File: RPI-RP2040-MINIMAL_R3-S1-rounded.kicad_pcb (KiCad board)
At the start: 2 copper layers, 65 x 46.7 mm, 34 parts, among them J1 Conn_01x03_Socket, J3 Conn_01x04_Pin, J4 Conn_01x04_Socket, P1 USB_C_Plug_USB2.0, U1 NCP1117ST33T3G, U2 W25Q128JVSIQ, U3 RP2040, X1 12MHz

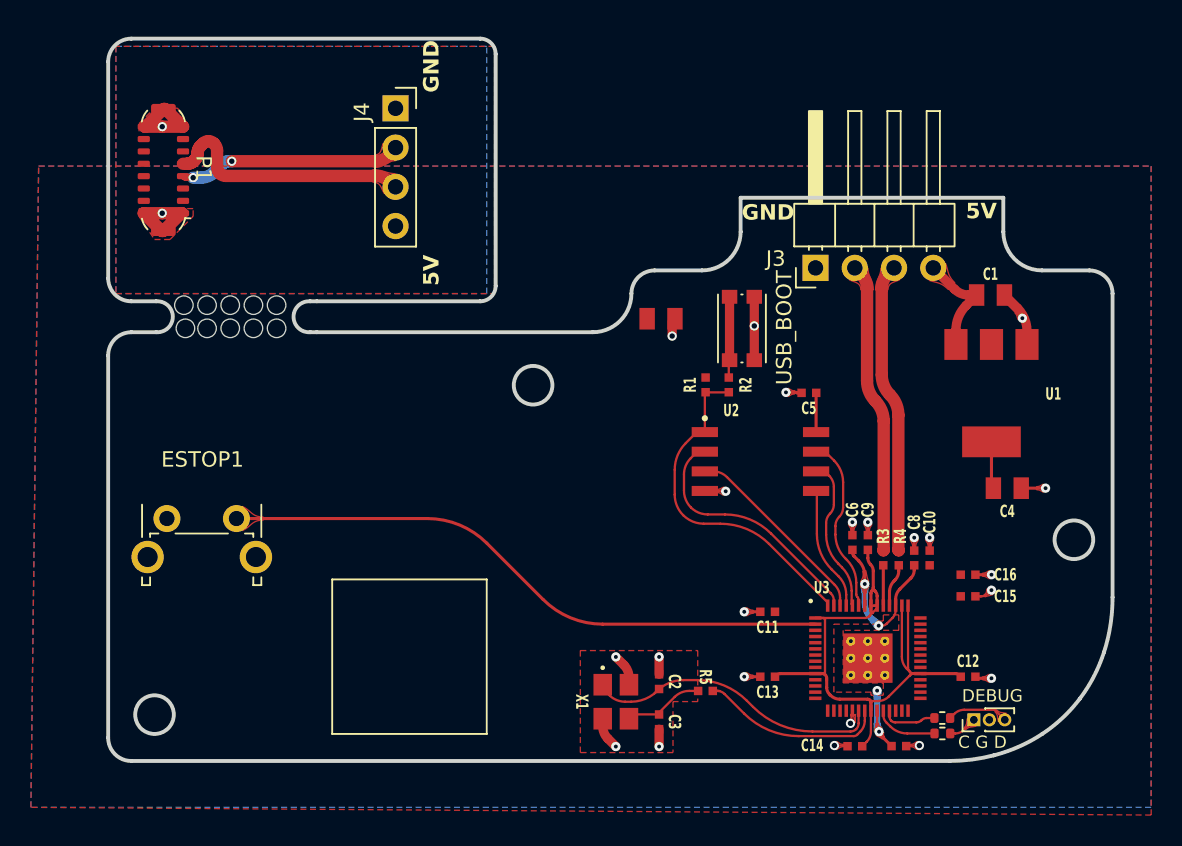
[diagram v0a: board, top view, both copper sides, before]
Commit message: attach both sides of port
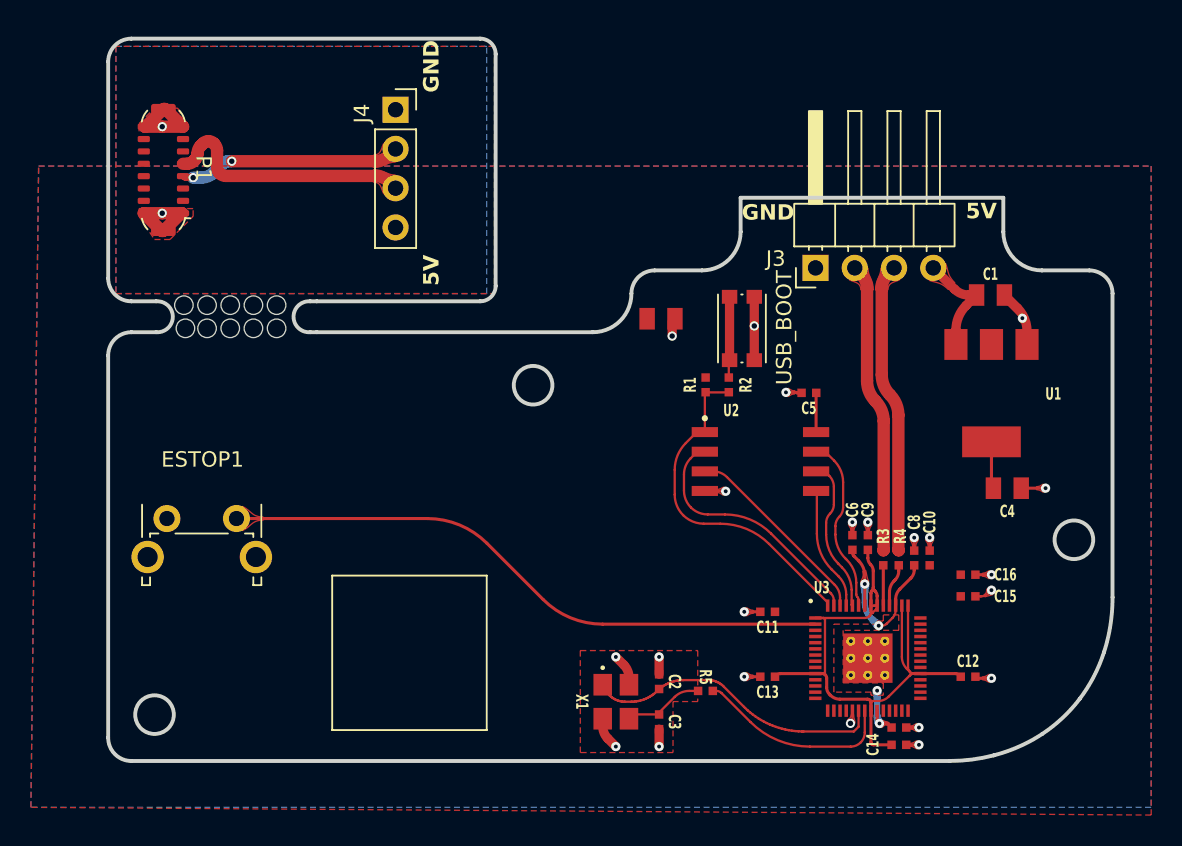
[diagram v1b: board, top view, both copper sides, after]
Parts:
- removed J1: Conn_01x03_Socket, Connector_PinHeader_1.00mm:PinHeader_1x03_P1.00mm_Vertical
- removed R6, R7: 100, Resistor_SMD:R_0402_1005Metric
- moved C14 2.85 mm to (101.7, 106.0), turned to 0 degrees
- moved C7 1.20 mm to (101.7, 104.8)
- moved J4 0.09 mm to (69.1, 64.9)
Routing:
- net /SWCLK: track 4.15 -> 0.00 mm
- net Net-(J1-Pin_3): track 3.98 -> 0.00 mm
- net /SWD: track 3.57 -> 0.00 mm
- net +1V1: track 17.1 -> 15.2 mm
- net Net-(J1-Pin_1): track 1.86 -> 0.00 mm
- net /BRIDGE_USBD-: track 18.1 -> 16.6 mm
- net +3V3: track 47.3 -> 48.0 mm
- net /XIN: track 19.6 -> 19.1 mm
- net /QSPI_SD2: track 12.8 -> 12.3 mm
- net /XOUT: track 12.4 -> 12.9 mm
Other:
- board text removed: "C G D"
- board text removed: "DEBUG"

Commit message: Rounding
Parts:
- added J1: Conn_01x03_Socket, Connector_PinHeader_1.00mm:PinHeader_1x03_P1.00mm_Vertical, F.Cu at (106.5, 104.3)
- added R6: 100, Resistor_SMD:R_0402_1005Metric, F.Cu at (104.5, 105.2)
- added R7: 100, Resistor_SMD:R_0402_1005Metric, F.Cu at (104.5, 104.2)
- moved C14 2.85 mm to (98.8, 106.0), turned to 180 degrees
- moved C7 1.20 mm to (101.7, 106.0)
- moved J4 0.09 mm to (69.1, 64.8)
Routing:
- net /SWCLK: track 0.00 -> 4.15 mm
- net Net-(J1-Pin_3): track 0.00 -> 3.98 mm
- net /SWD: track 0.00 -> 3.57 mm
- net +1V1: track 15.2 -> 17.1 mm
- net Net-(J1-Pin_1): track 0.00 -> 1.86 mm
- net /BRIDGE_USBD-: track 16.6 -> 18.1 mm
- net +3V3: track 48.0 -> 47.3 mm
- net /XIN: track 19.1 -> 19.6 mm
- net /QSPI_SD2: track 12.3 -> 12.8 mm
- net /XOUT: track 12.9 -> 12.4 mm
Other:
- board text added: "C G D"
- board text added: "DEBUG"
